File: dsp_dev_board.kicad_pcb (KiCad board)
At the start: 4 copper layers, 100 x 100 mm, 92 parts, among them J1 aux_mcu_power, J10 DX07S016JA1R1500, J11 Conn_02x11_Odd_Even, J2 audio_in, J3 audio_out, J4 9v_jack, J5 input_jack, J6 output_jack, J7 digital, J8 analog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

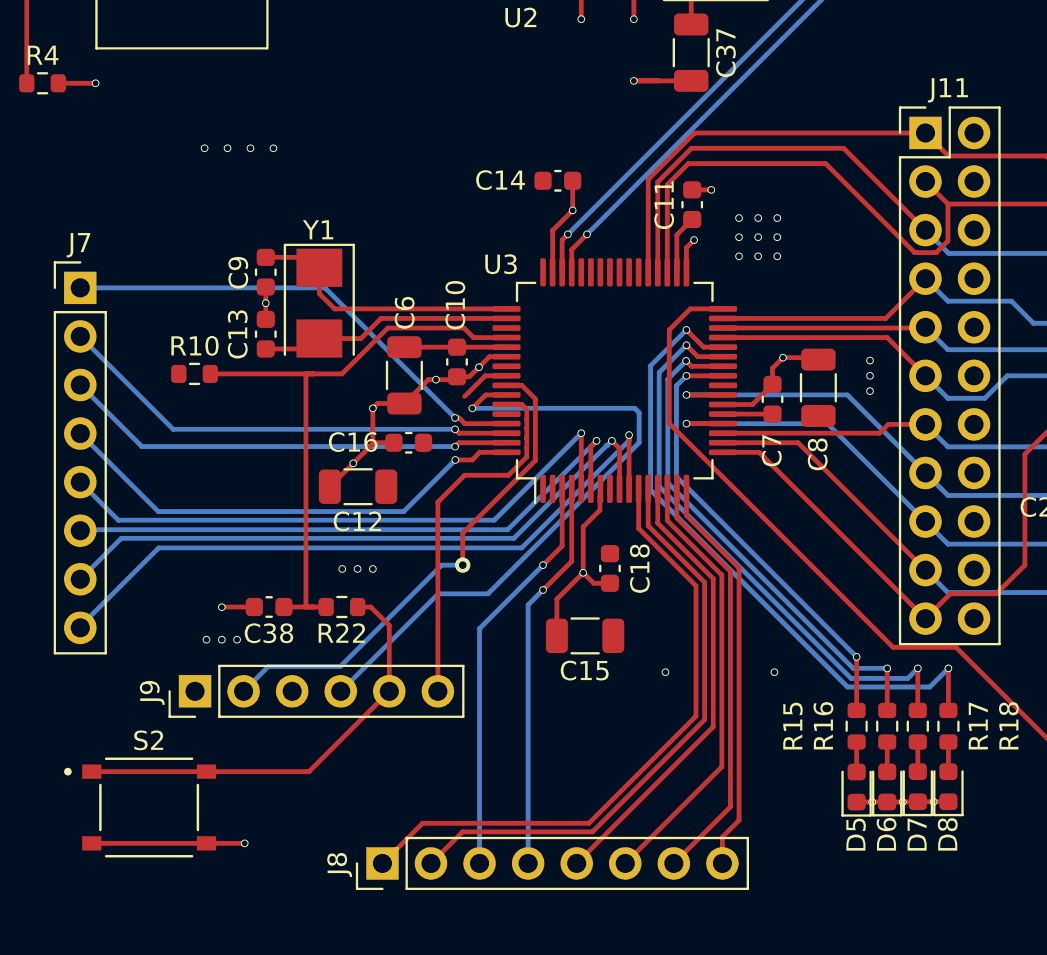
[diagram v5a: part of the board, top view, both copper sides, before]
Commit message: pcb: add silkscreens
This labels the pins for the analog, digital, debug, and probepoint
headers.  I also moved R10 so I could have more room for the digital
header labels.
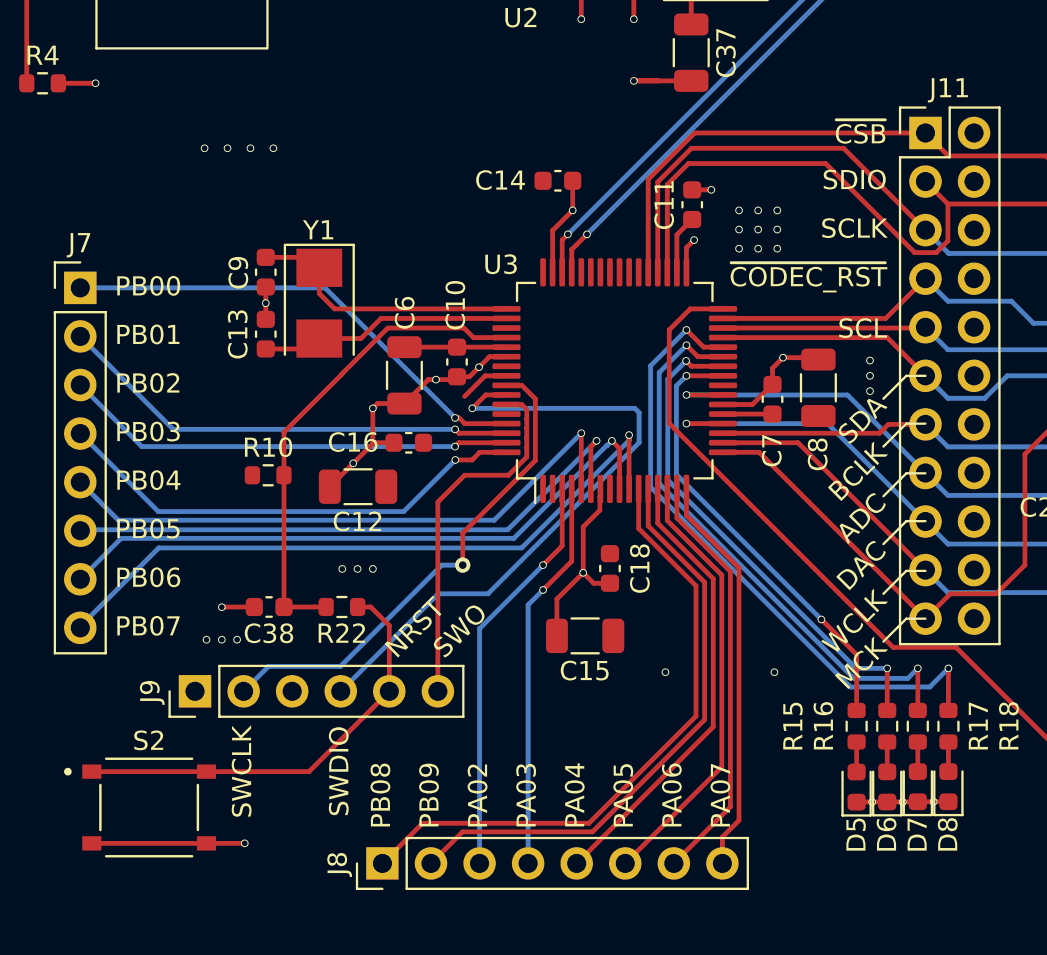
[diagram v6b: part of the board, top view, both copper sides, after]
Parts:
- moved R10 6.55 mm to (105.6, 89.5)
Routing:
- net Net-(C38-Pad1): track 31.9 -> 25.5 mm
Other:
- board text added: "ADC"
- board text added: "BCLK"
- board text added: "DAC"
- board text added: "MCK"
- board text added: "NRST"
- board text added: "PA02"
- board text added: "PA03"
- board text added: "PA04"
- board text added: "PA05"
- board text added: "PA06"
- board text added: "PA07"
- board text added: "PB00"
- board text added: "PB01"
- board text added: "PB02"
- board text added: "PB03"
- board text added: "PB04"
- board text added: "PB05"
- board text added: "PB06"
- board text added: "PB07"
- board text added: "PB08"
- board text added: "PB09"
- board text added: "SCL"
- board text added: "SCLK"
- board text added: "SDA"
- board text added: "SDIO"
- board text added: "SWCLK"
- board text added: "SWDIO"
- board text added: "SWO"
- board text added: "WCLK"
- board text added: "~CODEC_RST"
- board text added: "~CSB"
